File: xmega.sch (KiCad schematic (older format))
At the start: 32 parts, among them J1 USB, J2 PORTA, J3 PORTB, J4 PORTC, J5 PORTE, J7 POWER, U1 ATXMEGA128A1U-AU, U2 ADR380, U3 M24C02-WDW6TP

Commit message: Fix VBUS sense circuit
Voltage delivered with 2x(3k3) divider was too low, switch to 3x(3k3)
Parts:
- added unit 3 of R23
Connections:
- net GND: now also R23.6; no longer R23.2
- new net: R23.2, R23.3
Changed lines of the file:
@@
 	1150 7100 1300 7100
 Wire Wire Line
-	1300 7100 1300 7200
-Wire Wire Line
-	1300 7200 1300 7300
+	1300 7100 1300 7300
 Wire Wire Line
 	1300 7200 1200 7200
@@
 	9950 5000 9950 4950
 Wire Wire Line
-	7800 3400 9100 3400
-Wire Wire Line
-	9100 3400 9300 3400
+	7800 3400 9300 3400
 Connection ~ 9100 3400
 Wire Wire Line
-	8000 3200 8900 3200
-Wire Wire Line
-	8900 3200 9300 3200
-Wire Wire Line
-	7900 3300 8800 3300
-Wire Wire Line
-	8800 3300 9300 3300
+	8000 3200 9300 3200
+Wire Wire Line
+	7900 3300 9300 3300
 Wire Wire Line
 	9100 3500 9100 3400
@@
 	9250 3800 9100 3800
 Wire Wire Line
-	9100 3700 9100 3800
-Wire Wire Line
-	9100 3800 9100 3850
+	9100 3700 9100 3850
 $Comp
 L GND #PWR17
@@
 	10100 3200 10200 3200
 Wire Wire Line
-	10200 3200 10200 3300
-Wire Wire Line
-	10200 3300 10200 3400
-Wire Wire Line
-	10200 3400 10200 3500
-Wire Wire Line
-	10200 3500 10200 3550
+	10200 3200 10200 3550
 $Comp
 L GND #PWR20
@@
 $EndComp
 Wire Wire Line
-	2150 900  2500 900
-Wire Wire Line
-	2500 900  2850 900
+	2150 900  2850 900
 Wire Wire Line
 	2850 1000 2150 1000
@@
 	2800 800  2850 800
 Wire Wire Line
-	2150 2200 2600 2200
-Wire Wire Line
-	2600 2200 2850 2200
+	2150 2200 2850 2200
 Wire Wire Line
 	2850 2300 2150 2300
@@
 	2800 2100 2850 2100
 Wire Wire Line
-	700  3400 1100 3400
-Wire Wire Line
-	1100 3400 1250 3400
+	700  3400 1250 3400
 Wire Wire Line
 	1100 3400 1100 3500
@@
 Connection ~ 1100 3400
 Wire Wire Line
-	1950 3400 2000 3400
-Wire Wire Line
-	2000 3400 2200 3400
-Wire Wire Line
-	2200 3400 2250 3400
+	1950 3400 2250 3400
 Connection ~ 2000 3400
 Wire Wire Line
@@
 	3050 2860 7250 2860
 Wire Wire Line
-	1150 6700 1700 6700
-Wire Wire Line
-	1700 6700 2950 6700
-Wire Wire Line
-	2950 6700 9100 6700
+	1150 6700 9100 6700
 $Comp
 L DRTR5V0U2SR DZ1
@@
 $EndComp
 Wire Wire Line
-	1150 6800 2250 6800
-Wire Wire Line
-	2250 6800 3700 6800
+	1150 6800 3700 6800
 Wire Wire Line
 	1150 6900 3600 6900
@@
 	8800 6300 8900 6300
 Wire Wire Line
-	8900 6300 8900 6400
-Wire Wire Line
-	8900 6400 8900 6450
+	8900 6300 8900 6450
 $Comp
 L GND #PWR16
@@
 	-1   0    0    1
 $EndComp
-$Comp
-L GND #PWR15
-U 1 1 56F29687
-P 2950 7600
-F 0 "#PWR15" H 2950 7600 30  0001 C CNN
-F 1 "GND" H 2950 7530 30  0001 C CNN
-F 2 "" H 2950 7600 60  0000 C CNN
-F 3 "" H 2950 7600 60  0000 C CNN
-	1    2950 7600
-	1    0    0    -1
-$EndComp
 Wire Wire Line
 	2950 7600 2950 7550
 Wire Wire Line
-	2950 7350 2950 7250
-Wire Wire Line
-	2950 7250 2950 7150
+	2950 7150 2950 7350
 Wire Wire Line
 	2950 7250 3300 7250
@@
 	2250 7100 2250 6800
 Connection ~ 2250 6800
+$Comp
+L RESPACK-4X0603-CONV R23
+U 3 1 56F0E2C2
+P 2950 7700
+AR Path="/56F0E2C2" Ref="R23"  Part="3"
+AR Path="/56EFC605/56F0E2C2" Ref="R?"  Part="1"
+F 0 "R23" H 3013 7746 50  0000 L CNN
+F 1 "3k3" H 3013 7655 50  0000 L CNN
+F 2 "IPC7351-Nominal:RESCAXE80P160X320X70-8" H 2950 7700 50  0001 C CNN
+F 3 "" H 2950 7750 60  0000 C CNN
+F 4 "DIST DIGIKEY YC164J-3.3KCT-ND" H 2950 7700 60  0001 C CNN "BOM"
+	3    2950 7700
+	1    0    0    -1
+$EndComp
+$Comp
+L GND #PWR?
+U 1 1 56F0E371
+P 2950 7850
+F 0 "#PWR?" H 2950 7850 30  0001 C CNN
+F 1 "GND" H 2950 7780 30  0001 C CNN
+F 2 "" H 2950 7850 60  0000 C CNN
+F 3 "" H 2950 7850 60  0000 C CNN
+	1    2950 7850
+	1    0    0    -1
+$EndComp
+Wire Wire Line
+	2950 7850 2950 7800
 $EndSCHEMATC

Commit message: Decrease LED current
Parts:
- R23, R9: value 3k3 -> 15k; BOM DIST DIGIKEY YC164J-3.3KCT-ND -> DIST DIGIKEY YC164J-15KCT-ND
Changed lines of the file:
@@
 P 9950 4550
 F 0 "R9" H 9888 4504 50  0000 R CNN
-F 1 "3k3" H 9888 4595 50  0000 R CNN
+F 1 "15k" H 9888 4595 50  0000 R CNN
 F 2 "IPC7351-Nominal:RESCAXE80P160X320X70-8" H 9950 4550 50  0001 C CNN
 F 3 "" H 9950 4600 60  0000 C CNN
-F 4 "DIST DIGIKEY YC164J-3.3KCT-ND" H 9950 4550 60  0001 C CNN "BOM"
+F 4 "DIST DIGIKEY YC164J-15KCT-ND" H 9950 4550 60  0001 C CNN "BOM"
 	1    9950 4550
 	1    0    0    1
@@
 AR Path="/56EFC605/56F28A4A" Ref="R?"  Part="1"
 F 0 "R23" H 3013 7096 50  0000 L CNN
-F 1 "3k3" H 3013 7005 50  0000 L CNN
+F 1 "15k" H 3013 7005 50  0000 L CNN
 F 2 "IPC7351-Nominal:RESCAXE80P160X320X70-8" H 2950 7050 50  0001 C CNN
 F 3 "" H 2950 7100 60  0000 C CNN
-F 4 "DIST DIGIKEY YC164J-3.3KCT-ND" H 2950 7050 60  0001 C CNN "BOM"
+F 4 "DIST DIGIKEY YC164J-15KCT-ND" H 2950 7050 60  0001 C CNN "BOM"
 	1    2950 7050
 	1    0    0    -1
@@
 AR Path="/56EFC605/56F295D6" Ref="R?"  Part="1"
 F 0 "R23" H 2887 7404 50  0000 R CNN
-F 1 "3k3" H 2887 7495 50  0000 R CNN
+F 1 "15k" H 2887 7495 50  0000 R CNN
 F 2 "IPC7351-Nominal:RESCAXE80P160X320X70-8" H 2950 7450 50  0001 C CNN
 F 3 "" H 2950 7500 60  0000 C CNN
-F 4 "DIST DIGIKEY YC164J-3.3KCT-ND" H 2950 7450 60  0001 C CNN "BOM"
+F 4 "DIST DIGIKEY YC164J-15KCT-ND" H 2950 7450 60  0001 C CNN "BOM"
 	2    2950 7450
 	-1   0    0    1
@@
 AR Path="/56EFC605/56F0E2C2" Ref="R?"  Part="1"
 F 0 "R23" H 3013 7746 50  0000 L CNN
-F 1 "3k3" H 3013 7655 50  0000 L CNN
+F 1 "15k" H 3013 7655 50  0000 L CNN
 F 2 "IPC7351-Nominal:RESCAXE80P160X320X70-8" H 2950 7700 50  0001 C CNN
 F 3 "" H 2950 7750 60  0000 C CNN
-F 4 "DIST DIGIKEY YC164J-3.3KCT-ND" H 2950 7700 60  0001 C CNN "BOM"
+F 4 "DIST DIGIKEY YC164J-15KCT-ND" H 2950 7700 60  0001 C CNN "BOM"
 	3    2950 7700
 	1    0    0    -1

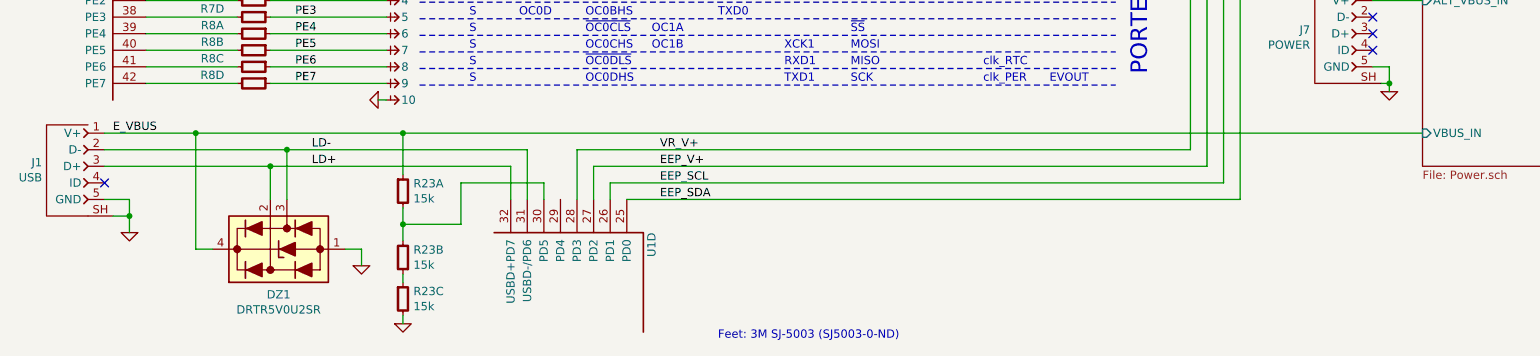
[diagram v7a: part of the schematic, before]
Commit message: Switch to passthrough USB TVS
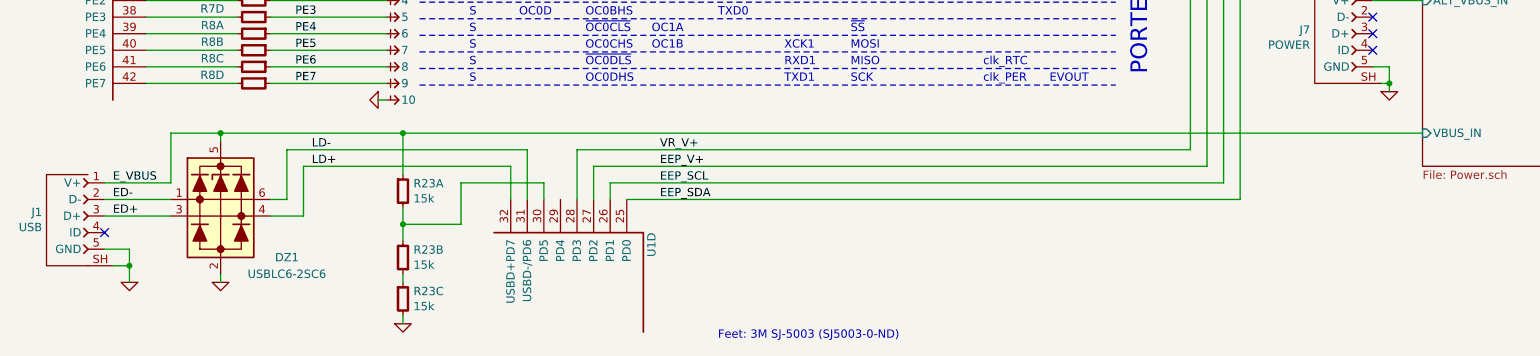
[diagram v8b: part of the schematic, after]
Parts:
- removed DZ1: DRTR5V0U2SR, smd-semi:SOT-143, symbol DRTR5V0U2SR
- added DZ1: USBLC6-2SC6, smd-semi:SOT-23-6, symbol USBLC6-2SC6
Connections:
- net E_VBUS: now also DZ1.5
- net GND: now also DZ1.2
- net LD+: now also DZ1.4; no longer J1.3 (D+)
- net LD-: now also DZ1.6; no longer J1.2 (D-)
- new net ED+: DZ1.3, J1.3 (D+)
- new net ED-: DZ1.1, J1.2 (D-)
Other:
- moved on the sheet: J1
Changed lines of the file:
@@
 L CONN-10118194-0001LF-UUSB-B J1
 U 1 1 56EBA7BF
-P 950 6900
-F 0 "J1" H 1127 6923 50  0000 L CNN
-F 1 "USB" H 1127 6832 50  0000 L CNN
-F 2 "conn-fci:CONN-10118194-0001LF-FCI" H 950 6900 50  0001 C CNN
-F 3 "" H 850 7100 50  0000 C CNN
-F 4 "DIST DIGIKEY 609-4618-1-ND" H 1450 7800 50  0001 C CNN "BOM"
-	1    950  6900
+P 950 7200
+F 0 "J1" H 1127 7223 50  0000 L CNN
+F 1 "USB" H 1127 7132 50  0000 L CNN
+F 2 "conn-fci:CONN-10118194-0001LF-FCI" H 950 7200 50  0001 C CNN
+F 3 "" H 850 7400 50  0000 C CNN
+F 4 "DIST DIGIKEY 609-4618-1-ND" H 1450 8100 50  0001 C CNN "BOM"
+	1    950  7200
 	-1   0    0    -1
 $EndComp
@@
 L GND #PWR2
 U 1 1 56EBAB34
-P 1300 7300
-F 0 "#PWR2" H 1300 7300 30  0001 C CNN
-F 1 "GND" H 1300 7230 30  0001 C CNN
-F 2 "" H 1300 7300 60  0000 C CNN
-F 3 "" H 1300 7300 60  0000 C CNN
-	1    1300 7300
+P 1300 7600
+F 0 "#PWR2" H 1300 7600 30  0001 C CNN
+F 1 "GND" H 1300 7530 30  0001 C CNN
+F 2 "" H 1300 7600 60  0000 C CNN
+F 3 "" H 1300 7600 60  0000 C CNN
+	1    1300 7600
 	-1   0    0    -1
 $EndComp
@@
 Feet: 3M SJ-5003 (SJ5003-0-ND)
 Wire Wire Line
-	1150 7100 1300 7100
-Wire Wire Line
-	1300 7100 1300 7300
-Wire Wire Line
-	1300 7200 1200 7200
-Connection ~ 1300 7200
+	1150 7400 1300 7400
+Wire Wire Line
+	1300 7400 1300 7600
+Wire Wire Line
+	1300 7500 1200 7500
+Connection ~ 1300 7500
 Wire Wire Line
 	9950 4750 9950 4650
@@
 Wire Wire Line
 	4000 6800 4000 7100
-Text Label 1200 6700 0    50   ~ 0
+Text Label 1200 7000 0    50   ~ 0
 E_VBUS
-NoConn ~ 1150 7000
+NoConn ~ 1150 7300
 $Comp
 L 24CXX-SOIC U3
@@
 $EndComp
 $Comp
-L GND #PWR4
+L GND #PWR5
 U 1 1 56EFF10A
 P 2000 3750
-AR Path="/56EFF10A" Ref="#PWR4"  Part="1"
+AR Path="/56EFF10A" Ref="#PWR5"  Part="1"
 AR Path="/56EF5090/56EFF10A" Ref="#PWR?"  Part="1"
-F 0 "#PWR4" H 2000 3750 30  0001 C CNN
+F 0 "#PWR5" H 2000 3750 30  0001 C CNN
 F 1 "GND" H 2000 3680 30  0001 C CNN
 F 2 "" H 2000 3750 60  0000 C CNN
@@
 	3050 2860 7250 2860
 Wire Wire Line
-	1150 6700 9100 6700
-$Comp
-L DRTR5V0U2SR DZ1
-U 1 1 56F0FA21
-P 2200 7400
-F 0 "DZ1" V 1926 7400 50  0000 C CNN
-F 1 "DRTR5V0U2SR" V 1835 7400 50  0000 C CNN
-F 2 "smd-semi:SOT-143" H 2200 6900 60  0001 C CNN
-F 3 "" H 2200 7350 60  0000 C CNN
-F 4 "TVS DIODESINC DRTR5V0U2SR" H 2200 6800 60  0001 C CNN "BOM"
-	1    2200 7400
-	0    -1   -1   0
-$EndComp
-Wire Wire Line
-	1150 6800 3700 6800
-Wire Wire Line
-	1150 6900 3600 6900
-Wire Wire Line
-	2150 6900 2150 7100
-Connection ~ 2150 6900
-Wire Wire Line
-	1800 7400 1700 7400
-$Comp
-L GND #PWR5
-U 1 1 56F10850
-P 2700 7500
-F 0 "#PWR5" H 2700 7500 30  0001 C CNN
-F 1 "GND" H 2700 7430 30  0001 C CNN
-F 2 "" H 2700 7500 60  0000 C CNN
-F 3 "" H 2700 7500 60  0000 C CNN
-	1    2700 7500
-	1    0    0    -1
-$EndComp
-Wire Wire Line
-	2700 7500 2700 7400
-Wire Wire Line
-	2700 7400 2600 7400
-Wire Wire Line
 	3600 6900 3600 7100
 Wire Wire Line
@@
 	3800 7000 3800 7100
 Connection ~ 2950 7250
-Wire Wire Line
-	1700 7400 1700 6700
-Connection ~ 1700 6700
-Wire Wire Line
-	2250 7100 2250 6800
-Connection ~ 2250 6800
 $Comp
 L RESPACK-4X0603-CONV R23
@@
 Wire Wire Line
 	2950 7850 2950 7800
+$Comp
+L USBLC6-2SC6 DZ1
+U 1 1 56FED3AE
+P 1850 7150
+F 0 "DZ1" H 2250 6850 50  0000 C CNN
+F 1 "USBLC6-2SC6" H 2250 6750 50  0000 C CNN
+F 2 "smd-semi:SOT-23-6" H 1850 6650 50  0001 C CNN
+F 3 "http://www.st.com/web/en/resource/technical/document/datasheet/CD00050750.pdf" H 1850 6450 50  0001 C CNN
+F 4 "TVS ST USBLC6-2SC6" H 1850 6550 50  0001 C CNN "BOM"
+	1    1850 7150
+	1    0    0    -1
+$EndComp
+Wire Wire Line
+	1150 7000 1550 7000
+Wire Wire Line
+	1550 7000 1550 6700
+Wire Wire Line
+	1550 6700 9100 6700
+Wire Wire Line
+	1850 6700 1850 6750
+Connection ~ 1850 6700
+Wire Wire Line
+	1150 7100 1550 7100
+Wire Wire Line
+	2150 7100 2250 7100
+Wire Wire Line
+	2250 7100 2250 6800
+Wire Wire Line
+	2250 6800 3700 6800
+Wire Wire Line
+	3600 6900 2350 6900
+Wire Wire Line
+	2350 6900 2350 7200
+Wire Wire Line
+	2350 7200 2150 7200
+Wire Wire Line
+	1550 7200 1150 7200
+$Comp
+L GND #PWR4
+U 1 1 56FEE4E2
+P 1850 7600
+F 0 "#PWR4" H 1850 7600 30  0001 C CNN
+F 1 "GND" H 1850 7530 30  0001 C CNN
+F 2 "" H 1850 7600 60  0000 C CNN
+F 3 "" H 1850 7600 60  0000 C CNN
+	1    1850 7600
+	1    0    0    -1
+$EndComp
+Wire Wire Line
+	1850 7600 1850 7550
+Text Label 1200 7100 0    50   ~ 0
+ED-
+Text Label 1200 7200 0    50   ~ 0
+ED+
 $EndSCHEMATC
